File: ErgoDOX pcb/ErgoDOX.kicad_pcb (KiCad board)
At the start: 2 copper layers, 182.8 x 158.9 mm, 72 parts, among them J1 USB, J2 3.5mm, J3 JMP, J4 JMP, SW0:10 SW0:3, SW0:11 SW0:2, SW0:12 SW0:1, SW0:7 SW0:6, SW0:8 SW0:5, SW0:9 SW0:4, SW1:10 SW1:3, SW1:11 SW1:2, SW1:12 SW1:1, SW1:13 SW1:0, SW1:9 SW1:4, SW2:10 SW2:3, SW2:11 SW2:2, SW2:12 SW2:1, SW2:13 SW2:0, SW2:7 SW2:6, SW2:8 SW2:5, SW2:9 SW2:4, SW3:10 SW3:3, SW3:11 SW3:2, SW3:12 SW3:1, SW3:13 SW3:0, SW3:8 SW3:5, SW3:9 SW3:4, SW4:10 SW4:3, SW4:11 SW4:2, SW4:12 SW4:1, SW4:13 SW4:0, SW4:7 SW4:6, SW4:8 SW4:5, SW4:9 SW4:4, SW5:10 SW5:3, SW5:11 SW5:2, SW5:12 SW5:1, SW5:13 SW5:0, SW5:7 SW5:6, SW5:8 SW5:5, SW5:9 SW5:4, U1 TEENSY2.0, U2 MCP23018

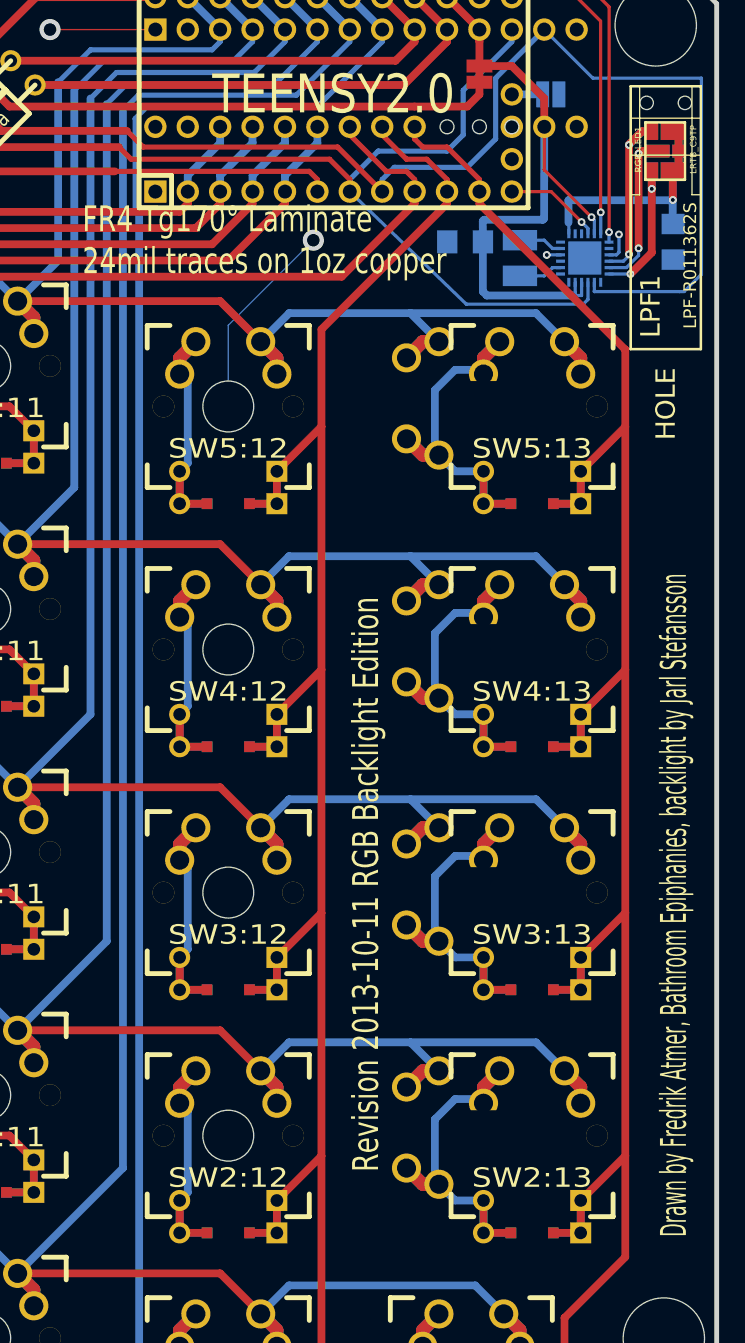
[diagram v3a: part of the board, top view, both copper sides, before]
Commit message: Fixed grounding issues and masks
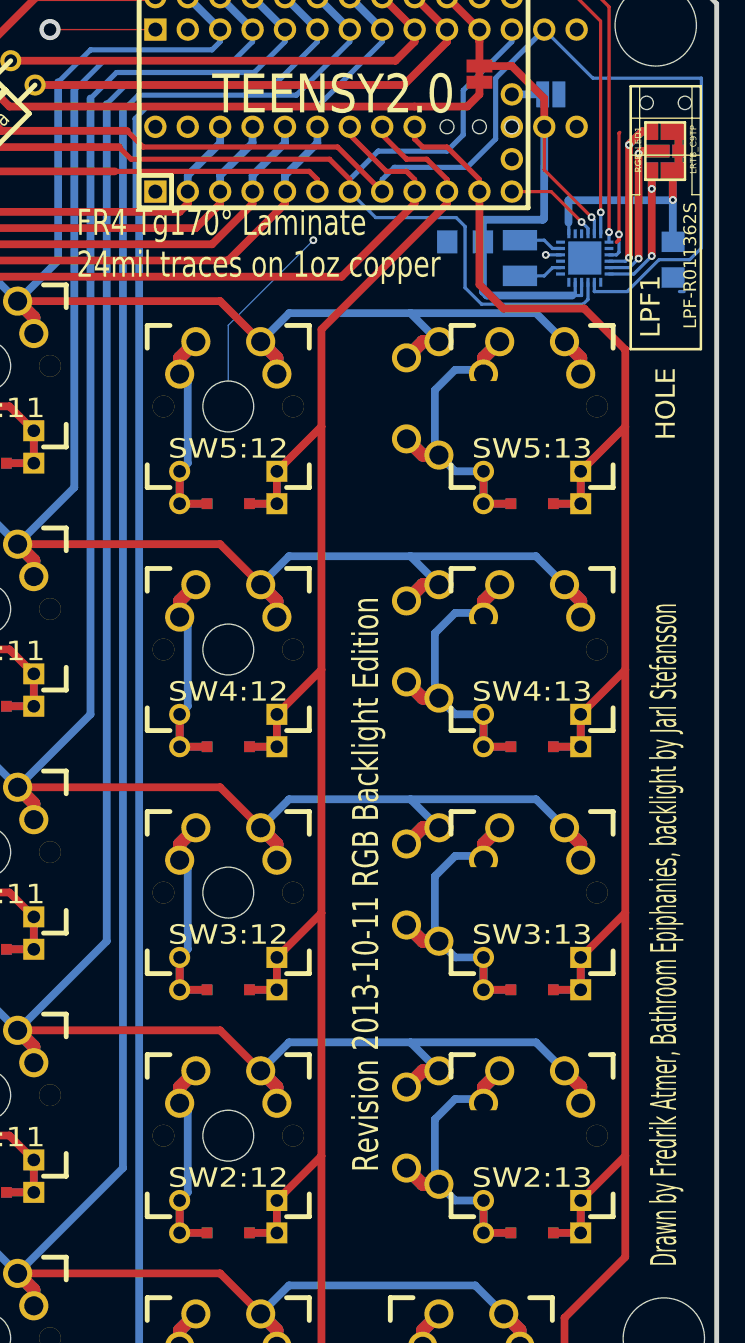
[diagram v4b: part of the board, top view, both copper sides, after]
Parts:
- moved COUT1 1.40 mm to (202.5, 55.5)
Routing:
- net GND: track 107.8 -> 116.6 mm
- net /COL0: track 159.7 -> 163.4 mm
- net /SCLM: track 143.6 -> 146.5 mm
- net /V_OUT_C_CATHODE: track 24.3 -> 25.8 mm
- net /SDAM: track 166.5 -> 165.3 mm
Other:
- board text added: "Design by Dominic Beauchamp, based on Key64 by Nestor A. Diaz"
- board text removed: "Design by Dominic Beauchamp, based on the Key64 by Nestor A. Diaz"

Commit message: AlmostReady
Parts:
- CIN1: value CAP 10 µF,6.3V/10V X7R -> CAP 10 µF
- L1: value INDUCTOR 2.2 µH, 1900 mA -> 2.2 µH, 1900 mA
- SW0:10, SW0:11, SW0:12, SW0:7, SW0:8, SW0:9, SW1:10, SW1:11, SW1:12, SW1:13, SW1:9, SW2:10, SW2:11, SW2:12, SW2:8, SW2:9, SW3:10, SW3:11, SW3:12, SW3:8, SW3:9, SW4:10, SW4:11, SW4:12, SW4:8, SW4:9, SW5:10, SW5:11, SW5:12, SW5:8, SW5:9: footprint MX_FLIP_DIODE -> MX_FLIP_DIODE_OPT
- SW2:13, SW3:13, SW4:13, SW5:13: footprint MX_FLIP_XX -> MX_FLIP_XX_OPT
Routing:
- net GND: track 116.6 -> 118.0 mm
